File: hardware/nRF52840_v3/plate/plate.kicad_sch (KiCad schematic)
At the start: 88 parts

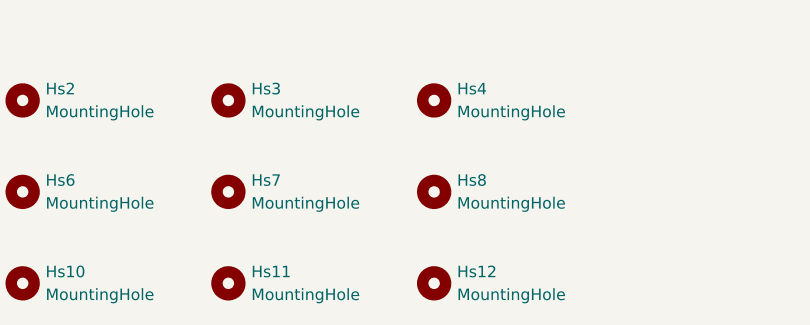
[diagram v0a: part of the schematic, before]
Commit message: M  hardware/nRF52840_v2/plate/plate.kicad_pcb M  hardware/nRF52840_v2/plate/plate.kicad_prl M  hardware/nRF52840_v2/plate/plate.kicad_pro A  hardware/nRF52840_v2/tmr-footprints/MountingHole_1.8mm_M1.6_NoPad.kicad_mod A  hardware/nRF52840_v2/tmr-footprints/MountingHole_2.2mm_M2.kicad_mod A  hardware/nRF52840_v2/tmr-footprints/SMTSO_M2.kicad_mod M  hardware/nRF52840_v3/border.py M  hardware/nRF52840_v3/pcb/pcb.kicad_pcb M  hardware/nRF52840_v3/pcb/pcb.kicad_prl M  hardware/nRF52840_v3/pcb/pcb.kicad_sch M  hardware/nRF52840_v3/placefp.py R  hardware/nRF52840_v2/plate/plate-Edge_Cuts.dxf -> hardware/nRF52840_v3/plate/plate-Edge_Cuts.dxf M  hardware/nRF52840_v3/plate/plate.kicad_pcb M  hardware/nRF52840_v3/plate/plate.kicad_prl M  hardware/nRF52840_v3/plate/plate.kicad_pro M  hardware/nRF52840_v3/plate/plate.kicad_sch A  hardware/nRF52840_v3/tmr-footprints/Aliexpress_SW_TACT_4x4x1.5mm.kicad_mod A  hardware/nRF52840_v3/tmr-footprints/MountingHole_1.8mm_M1.6_NoPad.kicad_mod A  hardware/nRF52840_v3/tmr-footprints/SMTSO_M2.kicad_mod M  hardware/nRF52840_v3/tmr-footprints/Stabilizer_Lowpro_2U.kicad_mod A  hardware/nRF52840_v3/tmr-footprints/USB_C_Receptacle_GCT_USB4085.kicad_mod
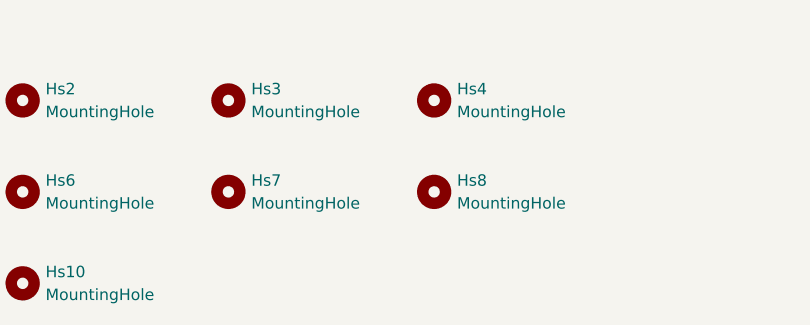
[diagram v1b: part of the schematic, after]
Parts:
- removed Hs11, Hs12: MountingHole, MountingHole:MountingHole_2.1mm, symbol Mechanical:MountingHole
- Hs1, Hs10, Hs2, Hs3, Hs4, Hs5, Hs6, Hs7, Hs8, Hs9: footprint MountingHole:MountingHole_2.1mm -> tmr-lib:MountingHole_1.8mm_M1.6_NoPad
- S57: footprint tmr-lib:Switch_Cutout_1.75u -> tmr-lib:Switch_Cutout
- S70: footprint tmr-lib:Switch_Cutout_1.25u -> tmr-lib:Switch_Cutout
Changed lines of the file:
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@@
 			)
 		)
-		(property "Footprint" "MountingHole:MountingHole_2.1mm"
+		(property "Footprint" "tmr-lib:MountingHole_1.8mm_M1.6_NoPad"
 			(at 115.57 133.35 0)
 			(effects
@@
 			)
 		)
-		(property "Footprint" "MountingHole:MountingHole_2.1mm"
+		(property "Footprint" "tmr-lib:MountingHole_1.8mm_M1.6_NoPad"
 			(at 161.29 133.35 0)
 			(effects
@@
 			)
 		)
-		(property "Footprint" "tmr-lib:Switch_Cutout_1.75u"
+		(property "Footprint" "tmr-lib:Switch_Cutout"
 			(at 194.31 78.74 0)
 			(effects
@@
 			)
 		)
-		(property "Footprint" "MountingHole:MountingHole_2.1mm"
+		(property "Footprint" "tmr-lib:MountingHole_1.8mm_M1.6_NoPad"
 			(at 93.98 123.19 0)
 			(effects
@@
 			)
 		)
-		(property "Footprint" "tmr-lib:Switch_Cutout_1.25u"
+		(property "Footprint" "tmr-lib:Switch_Cutout"
 			(at 182.88 91.44 0)
 			(effects
@@
 			)
 		)
-		(property "Footprint" "MountingHole:MountingHole_2.1mm"
+		(property "Footprint" "tmr-lib:MountingHole_1.8mm_M1.6_NoPad"
 			(at 138.43 133.35 0)
 			(effects
@@
 			)
 		)
-		(property "Footprint" "MountingHole:MountingHole_2.1mm"
+		(property "Footprint" "tmr-lib:MountingHole_1.8mm_M1.6_NoPad"
 			(at 115.57 143.51 0)
 			(effects
@@
 			)
 		)
-		(property "Footprint" "MountingHole:MountingHole_2.1mm"
+		(property "Footprint" "tmr-lib:MountingHole_1.8mm_M1.6_NoPad"
 			(at 115.57 123.19 0)
 			(effects
@@
 			)
 		)
-		(property "Footprint" "MountingHole:MountingHole_2.1mm"
+		(property "Footprint" "tmr-lib:MountingHole_1.8mm_M1.6_NoPad"
 			(at 138.43 123.19 0)
 			(effects
@@
 			)
 		)
-		(property "Footprint" "MountingHole:MountingHole_2.1mm"
+		(property "Footprint" "tmr-lib:MountingHole_1.8mm_M1.6_NoPad"
 			(at 93.98 143.51 0)
 			(effects
@@
 			)
 		)
-		(property "Footprint" "MountingHole:MountingHole_2.1mm"
+		(property "Footprint" "tmr-lib:MountingHole_1.8mm_M1.6_NoPad"
 			(at 93.98 133.35 0)
 			(effects
@@
 	)
 	(symbol
-		(lib_id "Mechanical:MountingHole")
-		(at 138.43 143.51 0)
-		(unit 1)
-		(exclude_from_sim no)
-		(in_bom no)
-		(on_board yes)
-		(dnp no)
-		(fields_autoplaced yes)
-		(property "Reference" "Hs11"
-			(at 140.97 142.2399 0)
-			(effects
-				(font
-					(size 1.27 1.27)
-				)
-				(justify left)
-			)
-		)
-		(property "Value" "MountingHole"
-			(at 140.97 144.7799 0)
-			(effects
-				(font
-					(size 1.27 1.27)
-				)
-				(justify left)
-			)
-		)
-		(property "Footprint" "MountingHole:MountingHole_2.1mm"
-			(at 138.43 143.51 0)
-			(effects
-				(font
-					(size 1.27 1.27)
-				)
-				(hide yes)
-			)
-		)
-		(property "Datasheet" "~"
-			(at 138.43 143.51 0)
-			(effects
-				(font
-					(size 1.27 1.27)
-				)
-				(hide yes)
-			)
-		)
-		(property "Description" "Mounting Hole without connection"
-			(at 138.43 143.51 0)
-			(effects
-				(font
-					(size 1.27 1.27)
-				)
-				(hide yes)
-			)
-		)
-		(instances
-			(project "plate"
-				(path "/4c67809e-1748-4898-89f6-ff92314048f2"
-					(reference "Hs11")
-					(unit 1)
-				)
-			)
-		)
-	)
-	(symbol
-		(lib_id "Mechanical:MountingHole")
-		(at 161.29 143.51 0)
-		(unit 1)
-		(exclude_from_sim no)
-		(in_bom no)
-		(on_board yes)
-		(dnp no)
-		(fields_autoplaced yes)
-		(property "Reference" "Hs12"
-			(at 163.83 142.2399 0)
-			(effects
-				(font
-					(size 1.27 1.27)
-				)
-				(justify left)
-			)
-		)
-		(property "Value" "MountingHole"
-			(at 163.83 144.7799 0)
-			(effects
-				(font
-					(size 1.27 1.27)
-				)
-				(justify left)
-			)
-		)
-		(property "Footprint" "MountingHole:MountingHole_2.1mm"
-			(at 161.29 143.51 0)
-			(effects
-				(font
-					(size 1.27 1.27)
-				)
-				(hide yes)
-			)
-		)
-		(property "Datasheet" "~"
-			(at 161.29 143.51 0)
-			(effects
-				(font
-					(size 1.27 1.27)
-				)
-				(hide yes)
-			)
-		)
-		(property "Description" "Mounting Hole without connection"
-			(at 161.29 143.51 0)
-			(effects
-				(font
-					(size 1.27 1.27)
-				)
-				(hide yes)
-			)
-		)
-		(instances
-			(project "plate"
-				(path "/4c67809e-1748-4898-89f6-ff92314048f2"
-					(reference "Hs12")
-					(unit 1)
-				)
-			)
-		)
-	)
-	(symbol
 		(lib_id "tmr-lib:SWHole")
 		(at 194.31 39.37 0)
@@
 			)
 		)
-		(property "Footprint" "MountingHole:MountingHole_2.1mm"
+		(property "Footprint" "tmr-lib:MountingHole_1.8mm_M1.6_NoPad"
 			(at 161.29 123.19 0)
 			(effects
